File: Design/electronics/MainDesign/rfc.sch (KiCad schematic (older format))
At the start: 24 parts, among them IC1 L298, IC2 L298, J1 CONN_02X20, J2 CONN_01X03, J3 CONN_01X03, M1 Motor, M2 Motor, M3 Motor, M4 Motor, U1 HC-SR04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

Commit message: Duck shoot changes to electronics design
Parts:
- removed U?: 1_Relay_Module, symbol 1_Relay_Module
- added J4: CONN_01X03, symbol CONN_01X03
- added M5: Motor, symbol Motor
- added U5: 2_Relay_Module, symbol 2_Relay_Module
- gave numbers to parts that had none: 1
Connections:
- net +12V: now also M5.2 (In2)
- net +5V: now also J4.2 (P2), U5.1 (+5v)
- net GND: now also J4.3 (P3), U5.10 (NO2), U5.2 (GND), U5.7 (NO1)
- net DUCK_SHOOT_MOTOR: now reaches J1.10 (P10)
- net DUCK_SHOOT_MOTOR: now also U5.4 (IN2)
- net DUCK_SHOOT_SERVO_FIRE: now reaches J1.13 (P13)
- net DUCK_SHOOT_LASER: now reaches J1.8 (P8)
- net DUCK_SHOOT_LASER: now also U5.3 (IN1)
- net at D1.1 (K): now also U5.6 (COM1)
- new net: M5.1 (In1), U5.9 (COM2)
- no-connect marks 20 -> 18
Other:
- note added: "Duck Shoot Control"
- note added: "GPIO12"
- note added: "GPIO13"
- note added: "GPIO14"
- note added: "GPIO15"
- note added: "GPIO16"
- note added: "GPIO17"
- note added: "GPIO18"
- note added: "GPIO19"
- note added: "GPIO20"
- note added: "GPIO22"
- note added: "GPIO23"
- note added: "GPIO24"
- note added: "GPIO25"
- note added: "GPIO26"
- note added: "GPIO27"
- note added: "GPIO4"
- note added: "GPIO5"
- note added: "GPIO6"
- note removed: "Laser Pointer"
- moved on the sheet: D1, IC1, IC2, J2, J3, M1, M2, M3, M4, R1, R2, R3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

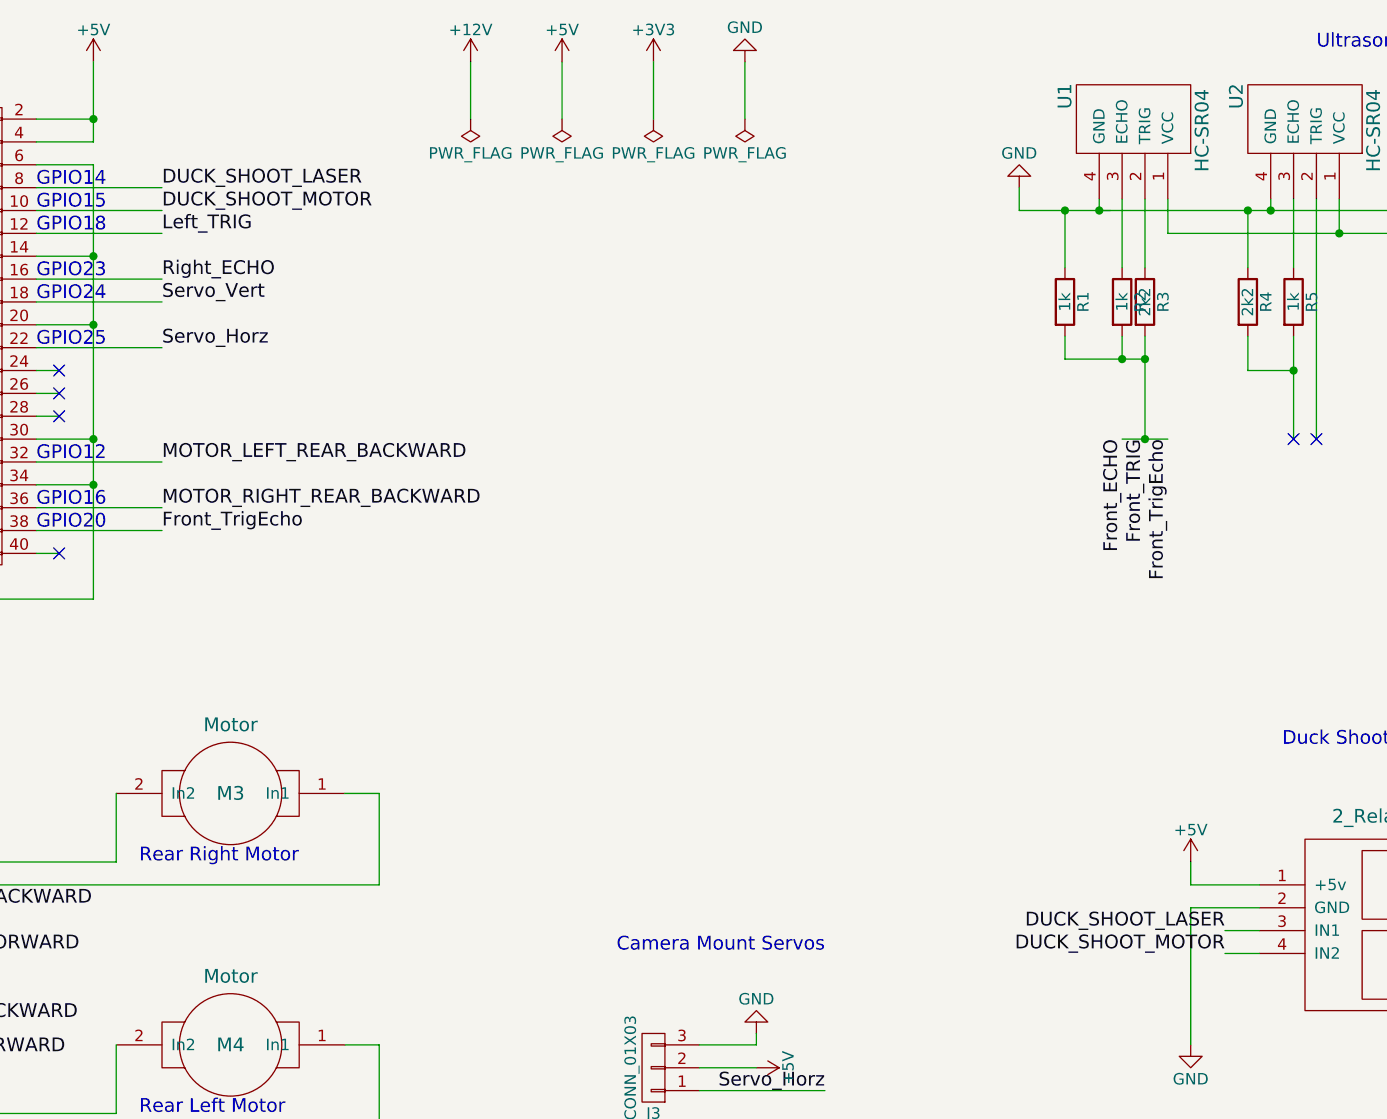
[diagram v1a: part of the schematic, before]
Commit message: Switched to using BCM (GPIO) numbering rather than pin (BOARD) numbering as a number of libraries use BCM and this was conflicting with the current definitions. (This was the cause of the runtime failure during testing today)
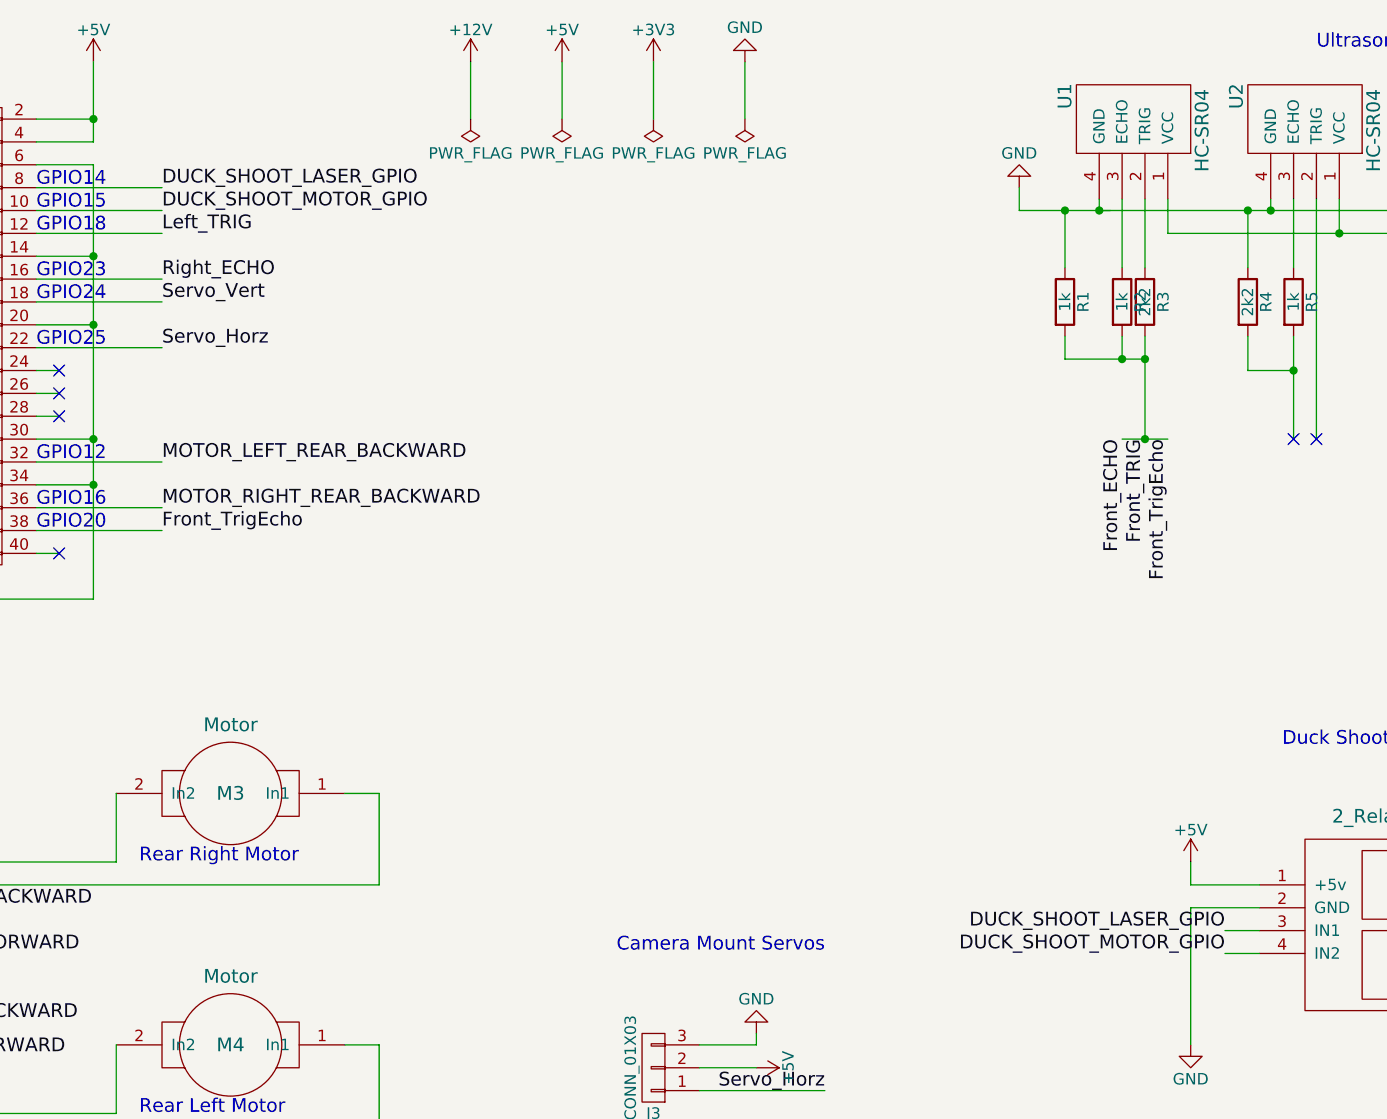
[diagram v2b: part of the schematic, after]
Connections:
- net DUCK_SHOOT_LASER renamed DUCK_SHOOT_LASER_GPIO
- net DUCK_SHOOT_MOTOR renamed DUCK_SHOOT_MOTOR_GPIO
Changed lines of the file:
@@
 	10700 4950 10700 4850
 Text Label 8400 4550 2    60   ~ 0
-DUCK_SHOOT_LASER
+DUCK_SHOOT_LASER_GPIO
 Text Label 8400 4650 2    60   ~ 0
-DUCK_SHOOT_MOTOR
+DUCK_SHOOT_MOTOR_GPIO
 Wire Wire Line
 	8400 4550 8550 4550
@@
 	8550 4650 8400 4650
 Text Label 3750 1400 0    60   ~ 0
-DUCK_SHOOT_MOTOR
+DUCK_SHOOT_MOTOR_GPIO
 NoConn ~ 9900 4250
 NoConn ~ 9900 4600
@@
 	3300 2900 3200 2900
 Text Label 3750 1300 0    60   ~ 0
-DUCK_SHOOT_LASER
+DUCK_SHOOT_LASER_GPIO
 Text Notes 3200 1300 0    60   ~ 0
 GPIO14

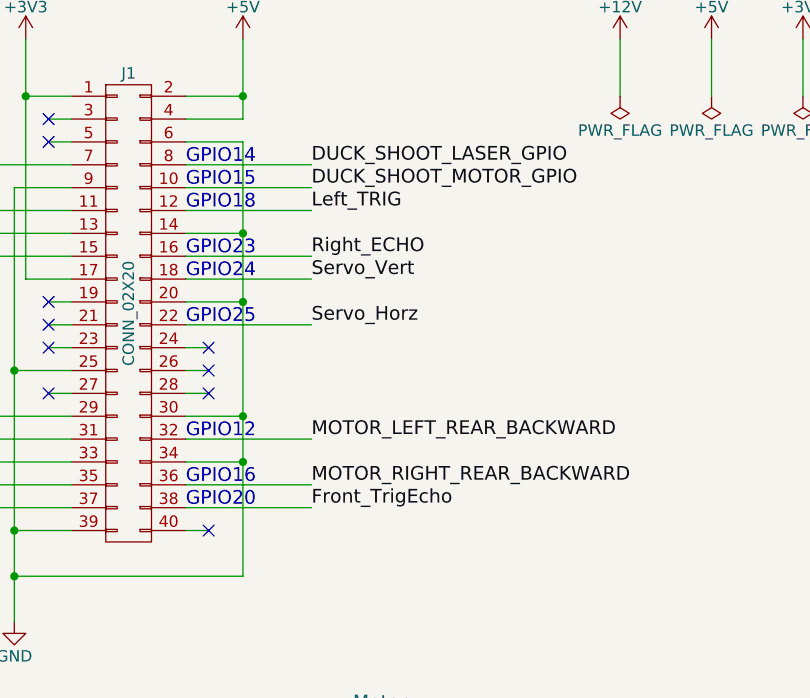
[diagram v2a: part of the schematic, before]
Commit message: updated gpio pin for the motor on off line
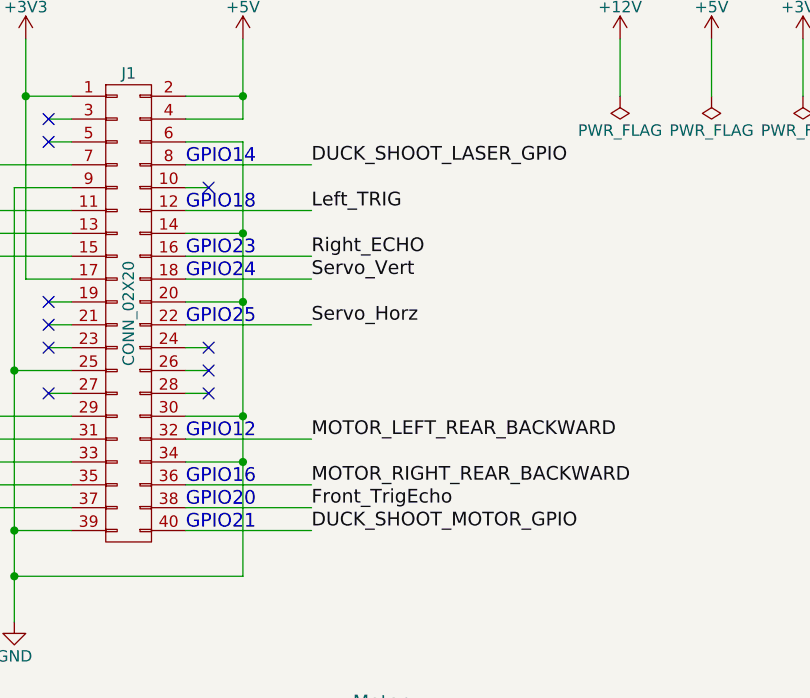
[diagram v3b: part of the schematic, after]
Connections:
- net DUCK_SHOOT_MOTOR_GPIO: now also J1.40 (P40); no longer J1.10 (P10)
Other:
- note added: "GPIO21"
- note removed: "GPIO15"
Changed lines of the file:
@@
 	3200 1300 3750 1300
-Wire Wire Line
-	3200 1400 3750 1400
 Wire Wire Line
 	1900 6250 1750 6250
@@
 Wire Wire Line
 	8550 4650 8400 4650
-Text Label 3750 1400 0    60   ~ 0
+Text Label 3750 2900 0    60   ~ 0
 DUCK_SHOOT_MOTOR_GPIO
 NoConn ~ 9900 4250
 NoConn ~ 9900 4600
-NoConn ~ 3300 2900
-Wire Wire Line
-	3300 2900 3200 2900
+Wire Wire Line
+	3200 2900 3750 2900
 Text Label 3750 1300 0    60   ~ 0
 DUCK_SHOOT_LASER_GPIO
 Text Notes 3200 1300 0    60   ~ 0
 GPIO14
-Text Notes 3200 1400 0    60   ~ 0
-GPIO15
+Text Notes 3200 2900 0    60   ~ 0
+GPIO21
 Text Notes 3200 1500 0    60   ~ 0
 GPIO18
@@
 Text Notes 2050 1300 0    60   ~ 0
 GPIO4
+NoConn ~ 3300 1400
+Wire Wire Line
+	3200 1400 3300 1400
 $EndSCHEMATC

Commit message: added web Links updated design files
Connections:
- net +12V: no longer M5.2 (In2)
- net +5V: no longer J4.2 (P2)
- new net +6V: J4.2 (P2), M5.2 (In2)
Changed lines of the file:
@@
-$EndComp
-$Comp
-L +5V #PWR026
-U 1 1 5A9C2783
-P 9400 5900
-F 0 "#PWR026" H 9400 5750 50  0001 C CNN
-F 1 "+5V" H 9400 6040 50  0000 C CNN
-F 2 "" H 9400 5900 50  0001 C CNN
-F 3 "" H 9400 5900 50  0001 C CNN
-	1    9400 5900
-	0    1    1    0
 $EndComp
 $Comp
@@
 	9400 5800 9150 5800
 Wire Wire Line
-	9150 5900 9400 5900
+	9150 5900 9700 5900
 Wire Wire Line
 	9150 6000 9700 6000
@@
 	1    0    0    -1
 $EndComp
-$Comp
-L +12V #PWR028
-U 1 1 5A9C915B
-P 10700 3700
-F 0 "#PWR028" H 10700 3550 50  0001 C CNN
-F 1 "+12V" H 10700 3840 50  0000 C CNN
-F 2 "" H 10700 3700 50  0001 C CNN
-F 3 "" H 10700 3700 50  0001 C CNN
-	1    10700 3700
-	1    0    0    -1
-$EndComp
-Wire Wire Line
-	10700 3700 10700 3850
 Wire Wire Line
 	9900 4800 10100 4800
@@
 Wire Wire Line
 	3200 1400 3300 1400
+$Comp
+L +6V #PWR?
+U 1 1 5ADB161A
+P 6700 750
+F 0 "#PWR?" H 6700 600 50  0001 C CNN
+F 1 "+6V" H 6700 890 50  0000 C CNN
+F 2 "" H 6700 750 50  0001 C CNN
+F 3 "" H 6700 750 50  0001 C CNN
+	1    6700 750
+	1    0    0    -1
+$EndComp
+$Comp
+L PWR_FLAG #FLG?
+U 1 1 5ADB1662
+P 6700 1000
+F 0 "#FLG?" H 6700 1075 50  0001 C CNN
+F 1 "PWR_FLAG" H 6700 1150 50  0000 C CNN
+F 2 "" H 6700 1000 50  0001 C CNN
+F 3 "" H 6700 1000 50  0001 C CNN
+	1    6700 1000
+	-1   0    0    1
+$EndComp
+Wire Wire Line
+	6700 750  6700 1000
+$Comp
+L +6V #PWR?
+U 1 1 5ADB17CF
+P 9700 5750
+F 0 "#PWR?" H 9700 5600 50  0001 C CNN
+F 1 "+6V" H 9700 5890 50  0000 C CNN
+F 2 "" H 9700 5750 50  0001 C CNN
+F 3 "" H 9700 5750 50  0001 C CNN
+	1    9700 5750
+	1    0    0    -1
+$EndComp
+Wire Wire Line
+	9700 5900 9700 5750
+$Comp
+L +6V #PWR?
+U 1 1 5ADB2477
+P 10700 3700
+F 0 "#PWR?" H 10700 3550 50  0001 C CNN
+F 1 "+6V" H 10700 3840 50  0000 C CNN
+F 2 "" H 10700 3700 50  0001 C CNN
+F 3 "" H 10700 3700 50  0001 C CNN
+	1    10700 3700
+	1    0    0    -1
+$EndComp
+Wire Wire Line
+	10700 3700 10700 3850
 $EndSCHEMATC
